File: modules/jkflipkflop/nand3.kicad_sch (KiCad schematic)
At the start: 6 parts, among them Q1 DMP3099L, Q2 2N7002, Q3 2N7002, Q4 2N7002, Q5 DMP3099L, Q6 DMP3099L

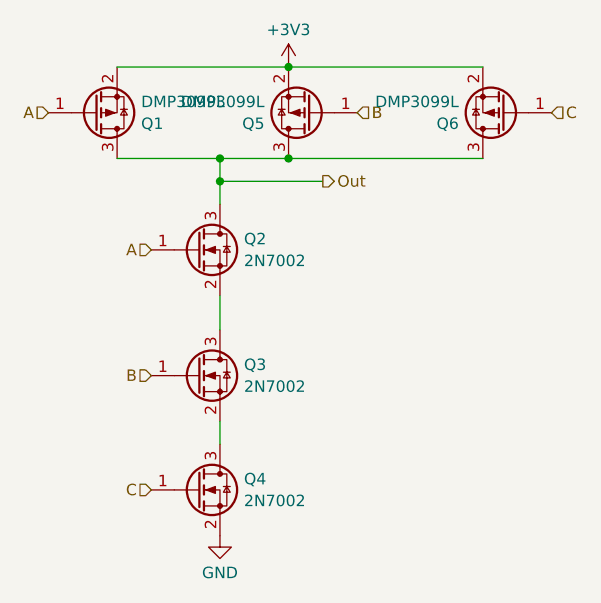
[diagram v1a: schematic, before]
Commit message: flipflop fab output
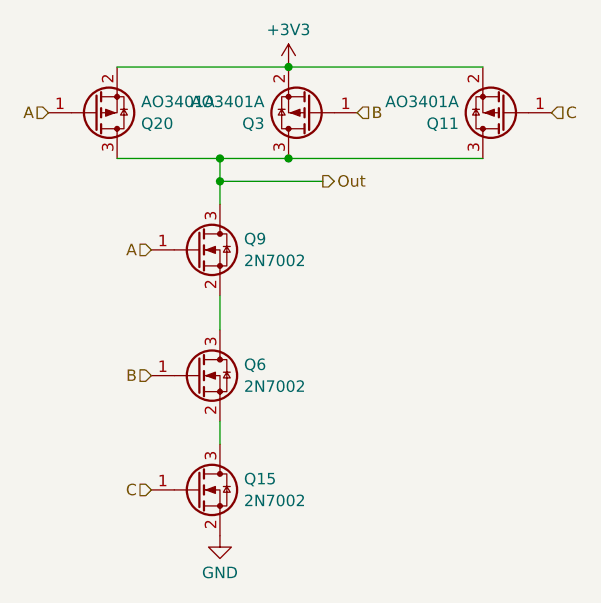
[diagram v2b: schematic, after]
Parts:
- Q11: renamed from Q6; value DMP3099L -> AO3401A; LCSC Part # (none) -> C15127
- Q15: renamed from Q4; LCSC Part # (none) -> C8545
- Q20: renamed from Q1; value DMP3099L -> AO3401A; LCSC Part # (none) -> C15127
- Q3: renamed from Q5; value DMP3099L -> AO3401A; LCSC Part # (none) -> C15127
- Q6: renamed from Q3; LCSC Part # (none) -> C8545
- Q9: renamed from Q2; LCSC Part # (none) -> C8545
